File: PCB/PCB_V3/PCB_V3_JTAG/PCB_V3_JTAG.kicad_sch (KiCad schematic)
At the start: 84 parts, among them J1 ESP_Left, J10 MCP_RIGHT, J11 ACS2_pins, J12 ACS4_Pins, J13 ACS2_Screw, J14 ACS4_Screw, J15 MCP_VCC_LINE, J16 AMS_IP_Pins, J17 AMS_OP_Pins, J18 BC1_IN+, J19 BC1_IN-, J2 ESP_Right, J20 BC3_IN+, J21 BC3_IN-, J22 BC1_OUT+, J23 BC1_OUT-, J24 BC3_OUT+, J25 BC3_OUT-, J26 BC2_IN+, J27 BC2_IN-, J28 BC5_IN+, J29 BC5_IN-, J3 ACS1_Pins, J30 BC2_OUT+, J31 BC2_OUT-, J32 BC5_OUT+, J33 BC5_OUT-, J34 Left_LED_1, J35 Left_LED_2, J36 Left_LED_3, J37 Left_LED_4, J38 Left_LED_5, J39 Right_LED_1, J4 ACS3_Pins, J40 Right_LED_2, J41 Right_LED_3, J42 Right_LED_4, J43 Right_LED_5, J44 STATIC_LED_1, J45 STATIC_LED_2, J46 I/P_Terminal, J47 Battery_Terminal, J5 ACS3_Screw, J6 ACS1_Screw, J7 LAN_Pins_2, J8 MCP_LEFT, J9 LAN_Pins_1, Q1 IRLZ44N, Q10 IRLZ44N, Q2 IRLZ44N, Q3 IRLZ44N, Q4 IRLZ44N, Q5 IRLZ44N, Q6 IRLZ44N, Q7 IRLZ44N, Q8 IRLZ44N, Q9 IRLZ44N

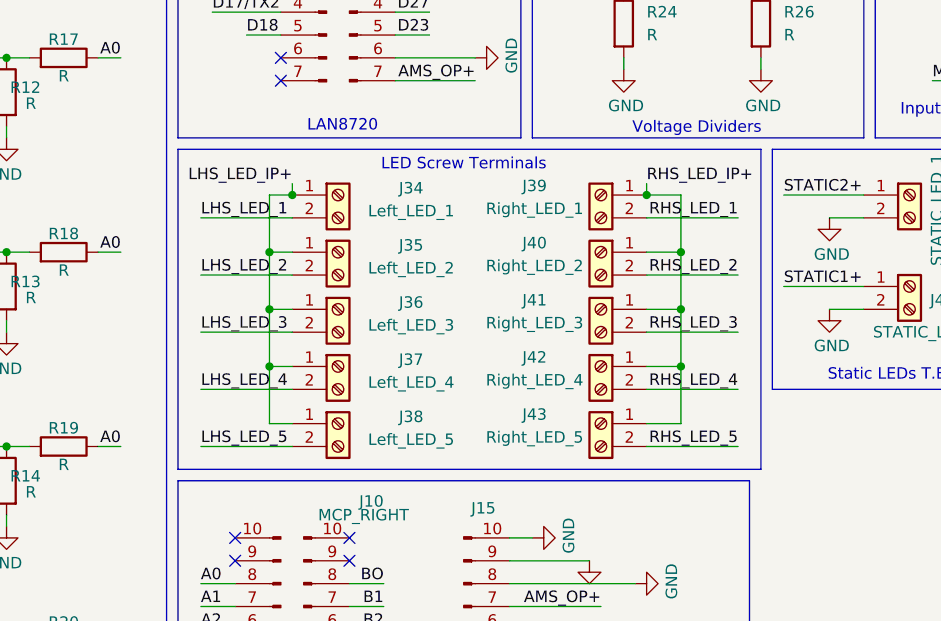
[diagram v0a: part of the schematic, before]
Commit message: Uploading the JTAG files and updated the footprints for the resistors
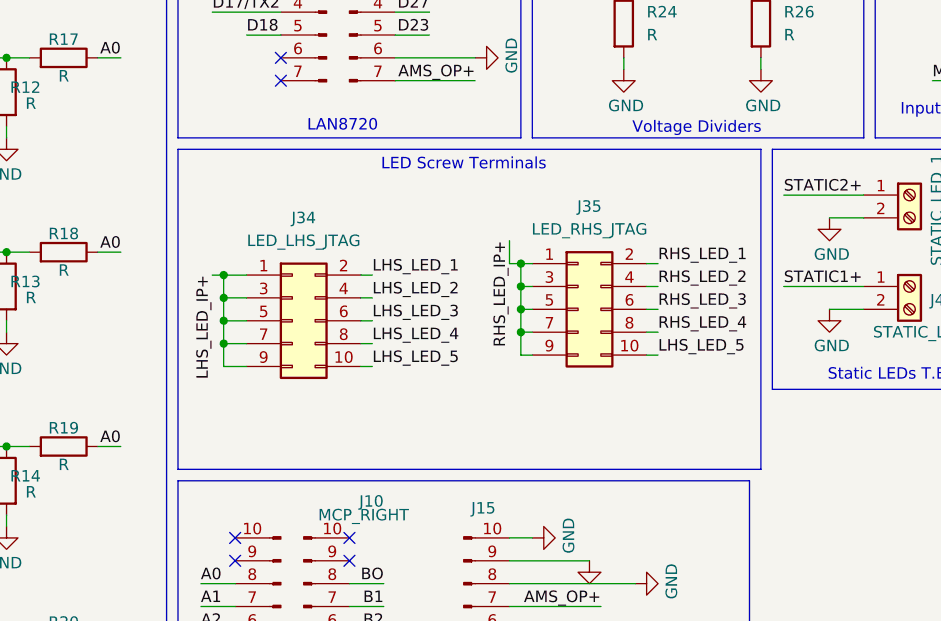
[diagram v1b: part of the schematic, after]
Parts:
- removed J34: Left_LED_1, TerminalBlock_Phoenix:TerminalBlock_Phoenix_MKDS-1,5-2-5.08_1x02_P5.08mm_Horizontal, symbol Connector:Screw_Terminal_01x02
- removed J35: Left_LED_2, TerminalBlock_Phoenix:TerminalBlock_Phoenix_MKDS-1,5-2-5.08_1x02_P5.08mm_Horizontal, symbol Connector:Screw_Terminal_01x02
- removed J36: Left_LED_3, TerminalBlock_Phoenix:TerminalBlock_Phoenix_MKDS-1,5-2-5.08_1x02_P5.08mm_Horizontal, symbol Connector:Screw_Terminal_01x02
- removed J37: Left_LED_4, TerminalBlock_Phoenix:TerminalBlock_Phoenix_MKDS-1,5-2-5.08_1x02_P5.08mm_Horizontal, symbol Connector:Screw_Terminal_01x02
- removed J38: Left_LED_5, TerminalBlock_Phoenix:TerminalBlock_Phoenix_MKDS-1,5-2-5.08_1x02_P5.08mm_Horizontal, symbol Connector:Screw_Terminal_01x02
- removed J39: Right_LED_1, TerminalBlock_Phoenix:TerminalBlock_Phoenix_MKDS-1,5-2-5.08_1x02_P5.08mm_Horizontal, symbol Connector:Screw_Terminal_01x02
- removed J40: Right_LED_2, TerminalBlock_Phoenix:TerminalBlock_Phoenix_MKDS-1,5-2-5.08_1x02_P5.08mm_Horizontal, symbol Connector:Screw_Terminal_01x02
- removed J41: Right_LED_3, TerminalBlock_Phoenix:TerminalBlock_Phoenix_MKDS-1,5-2-5.08_1x02_P5.08mm_Horizontal, symbol Connector:Screw_Terminal_01x02
- removed J42: Right_LED_4, TerminalBlock_Phoenix:TerminalBlock_Phoenix_MKDS-1,5-2-5.08_1x02_P5.08mm_Horizontal, symbol Connector:Screw_Terminal_01x02
- removed J43: Right_LED_5, TerminalBlock_Phoenix:TerminalBlock_Phoenix_MKDS-1,5-2-5.08_1x02_P5.08mm_Horizontal, symbol Connector:Screw_Terminal_01x02
- added J34: LED_LHS_JTAG, Connector_PinSocket_2.54mm:PinSocket_2x05_P2.54mm_Vertical, symbol Connector_Generic:Conn_02x05_Odd_Even
- added J35: LED_RHS_JTAG, Connector_PinSocket_2.54mm:PinSocket_2x05_P2.54mm_Vertical, symbol Connector_Generic:Conn_02x05_Odd_Even
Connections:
- net LHS_LED_1: now also J34.2 (Pin_2)
- net LHS_LED_2: now also J34.4 (Pin_4)
- net LHS_LED_3: now also J34.6 (Pin_6)
- net LHS_LED_4: now also J34.8 (Pin_8)
- net LHS_LED_5: now also J34.10 (Pin_10), J35.10 (Pin_10)
- net LHS_LED_IP+: now also J34.1 (Pin_1), J34.3 (Pin_3), J34.5 (Pin_5), J34.7 (Pin_7), J34.9 (Pin_9)
- net RHS_LED_1: now also J35.2 (Pin_2)
- net RHS_LED_2: now also J35.4 (Pin_4)
- net RHS_LED_3: now also J35.6 (Pin_6)
- net RHS_LED_4: now also J35.8 (Pin_8)
- net RHS_LED_IP+: now also J35.1 (Pin_1), J35.3 (Pin_3), J35.5 (Pin_5), J35.7 (Pin_7), J35.9 (Pin_9)
